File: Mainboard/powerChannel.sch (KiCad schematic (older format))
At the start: 2 parts, among them Q5 IRL640

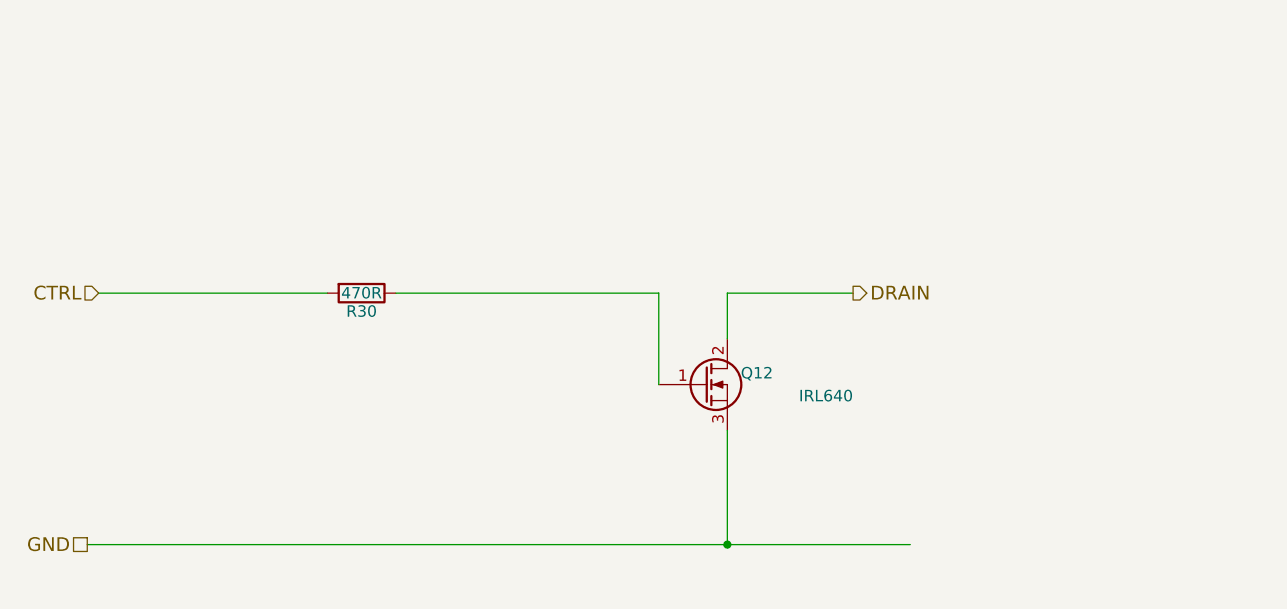
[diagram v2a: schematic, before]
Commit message: Made I2C level converters more neat
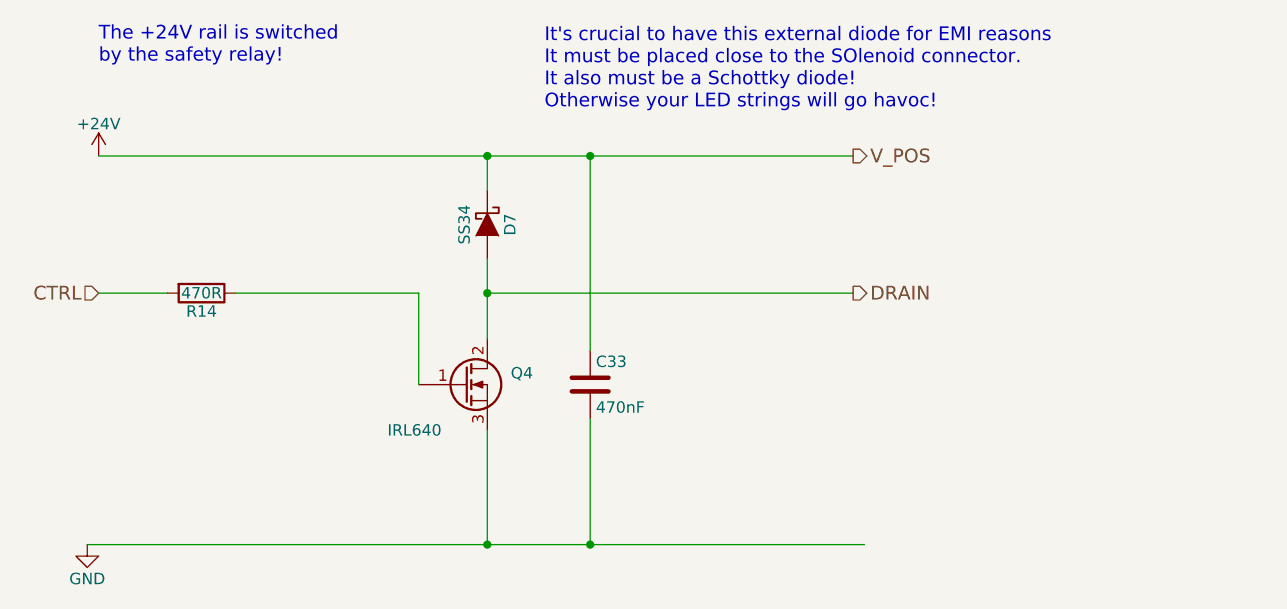
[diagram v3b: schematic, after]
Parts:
- added C25: 470nF, Capacitors_SMD:C_0805_HandSoldering, symbol C
- added D8: SS34, Diodes_SMD:SMC-RM10_Universal_Handsoldering, symbol D_Schottky
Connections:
- net labels added: +24V, V_POS
- wire segments 7 -> 11
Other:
- note added: "It's crucial to have this external diode for EMI reasons\nIt must be placed close to the SOlenoid connector.\nIt also must be a Schottky diode!\nOtherwise your LED strings will go havoc!"
- note added: "The +24V rail is switched\nby the safety relay!"
- moved on the sheet: Q4, R14
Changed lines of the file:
@@
 $Descr A4 11693 8268
 encoding utf-8
-Sheet 7 14
+Sheet 19 19
 Title ""
 Date ""
@@
 Text HLabel 1850 3600 0    60   Input ~ 0
 CTRL
-Text HLabel 1800 4700 0    60   UnSpc ~ 0
-GND
 Text HLabel 5150 3600 2    60   Output ~ 0
 DRAIN
 Wire Wire Line
-	1800 4700 5400 4700
-Wire Wire Line
-	4600 4200 4600 4700
-Connection ~ 4600 4700
-Wire Wire Line
-	4600 3800 4600 3600
-Wire Wire Line
-	4600 3600 5150 3600
-Wire Wire Line
-	4300 3600 4300 4000
+	1800 4700 5200 4700
+Wire Wire Line
+	3550 4200 3550 4700
+Connection ~ 3550 4700
+Wire Wire Line
+	3550 3450 3550 3800
+Wire Wire Line
+	3250 3600 3250 4000
 $Comp
 L R R23
 U 1 1 567075BF
-P 3000 3600
+P 2300 3600
 AR Path="/56721A83/567075BF" Ref="R23"  Part="1"
 AR Path="/56721A88/567075BF" Ref="R24"  Part="1"
@@
 AR Path="/56723FA7/567075BF" Ref="R29"  Part="1"
 AR Path="/56723FAC/567075BF" Ref="R30"  Part="1"
-F 0 "R30" V 3080 3600 50  0000 C CNN
-F 1 "470R" V 3000 3600 50  0000 C CNN
-F 2 "Resistors_SMD:R_0805_HandSoldering" V 2930 3600 50  0001 C CNN
-F 3 "" H 3000 3600 50  0000 C CNN
-	1    3000 3600
+AR Path="/57745597/567075BF" Ref="R24"  Part="1"
+AR Path="/577458A1/567075BF" Ref="R25"  Part="1"
+AR Path="/57745BCF/567075BF" Ref="R26"  Part="1"
+AR Path="/577510FE/567075BF" Ref="R27"  Part="1"
+AR Path="/57751111/567075BF" Ref="R28"  Part="1"
+AR Path="/57751116/567075BF" Ref="R29"  Part="1"
+AR Path="/5775111B/567075BF" Ref="R30"  Part="1"
+AR Path="/5770A9F1/567075BF" Ref="R1"  Part="1"
+AR Path="/5770AA04/567075BF" Ref="R24"  Part="1"
+AR Path="/5770AA09/567075BF" Ref="R24"  Part="1"
+AR Path="/5770AA0E/567075BF" Ref="R24"  Part="1"
+AR Path="/57714FDB/567075BF" Ref="R2"  Part="1"
+AR Path="/57715882/567075BF" Ref="R5"  Part="1"
+AR Path="/57715887/567075BF" Ref="R14"  Part="1"
+F 0 "R14" V 2380 3600 50  0000 C CNN
+F 1 "470R" V 2300 3600 50  0000 C CNN
+F 2 "Resistors_SMD:R_0805_HandSoldering" V 2230 3600 50  0001 C CNN
+F 3 "" H 2300 3600 50  0000 C CNN
+	1    2300 3600
 	0    1    1    0
 $EndComp
-Wire Wire Line
-	1850 3600 2850 3600
-Wire Wire Line
-	3150 3600 4300 3600
 $Comp
 L Q_NMOS_GDS Q5
 U 1 1 56763CC0
-P 4500 4000
+P 3450 4000
 AR Path="/56721A83/56763CC0" Ref="Q5"  Part="1"
 AR Path="/56721A88/56763CC0" Ref="Q6"  Part="1"
@@
 AR Path="/56723FA7/56763CC0" Ref="Q11"  Part="1"
 AR Path="/56723FAC/56763CC0" Ref="Q12"  Part="1"
-F 0 "Q12" H 4800 4050 50  0000 R CNN
-F 1 "IRL640" H 5150 3950 50  0000 R CNN
-F 2 "TO_SOT_Packages_THT:TO-220_Neutral123_Vertical_LargePads" H 4700 4100 50  0001 C CNN
-F 3 "" H 4500 4000 50  0000 C CNN
-	1    4500 4000
-	1    0    0    -1
-$EndComp
+AR Path="/57745597/56763CC0" Ref="Q6"  Part="1"
+AR Path="/577458A1/56763CC0" Ref="Q7"  Part="1"
+AR Path="/57745BCF/56763CC0" Ref="Q8"  Part="1"
+AR Path="/577510FE/56763CC0" Ref="Q9"  Part="1"
+AR Path="/57751111/56763CC0" Ref="Q10"  Part="1"
+AR Path="/57751116/56763CC0" Ref="Q11"  Part="1"
+AR Path="/5775111B/56763CC0" Ref="Q12"  Part="1"
+AR Path="/5770A9F1/56763CC0" Ref="Q1"  Part="1"
+AR Path="/5770AA04/56763CC0" Ref="Q6"  Part="1"
+AR Path="/5770AA09/56763CC0" Ref="Q6"  Part="1"
+AR Path="/5770AA0E/56763CC0" Ref="Q6"  Part="1"
+AR Path="/57714FDB/56763CC0" Ref="Q2"  Part="1"
+AR Path="/57715882/56763CC0" Ref="Q3"  Part="1"
+AR Path="/57715887/56763CC0" Ref="Q4"  Part="1"
+F 0 "Q4" H 3750 4050 50  0000 R CNN
+F 1 "IRL640" H 3350 3800 50  0000 R CNN
+F 2 "TO_SOT_Packages_THT:TO-220_Neutral123_Vertical_LargePads" H 3650 4100 50  0001 C CNN
+F 3 "" H 3450 4000 50  0000 C CNN
+	1    3450 4000
+	1    0    0    -1
+$EndComp
+Wire Wire Line
+	1850 3600 2150 3600
+Wire Wire Line
+	2450 3600 3250 3600
+Text Notes 3800 2800 0    60   ~ 0
+It's crucial to have this external diode for EMI reasons\nIt must be placed close to the SOlenoid connector.\nIt also must be a Schottky diode!\nOtherwise your LED strings will go havoc!
+Wire Wire Line
+	1850 3000 5150 3000
+Wire Wire Line
+	3550 3150 3550 3000
+Connection ~ 3550 3000
+$Comp
+L D_Schottky D8
+U 1 1 5772D520
+P 3550 3300
+AR Path="/56721A83/5772D520" Ref="D8"  Part="1"
+AR Path="/56721A88/5772D520" Ref="D?"  Part="1"
+AR Path="/57745597/5772D520" Ref="D9"  Part="1"
+AR Path="/577458A1/5772D520" Ref="D10"  Part="1"
+AR Path="/57745BCF/5772D520" Ref="D11"  Part="1"
+AR Path="/577510FE/5772D520" Ref="D13"  Part="1"
+AR Path="/57751111/5772D520" Ref="D14"  Part="1"
+AR Path="/57751116/5772D520" Ref="D15"  Part="1"
+AR Path="/5775111B/5772D520" Ref="D16"  Part="1"
+AR Path="/5770A9F1/5772D520" Ref="D4"  Part="1"
+AR Path="/5770AA04/5772D520" Ref="D9"  Part="1"
+AR Path="/5770AA09/5772D520" Ref="D9"  Part="1"
+AR Path="/5770AA0E/5772D520" Ref="D9"  Part="1"
+AR Path="/57714FDB/5772D520" Ref="D5"  Part="1"
+AR Path="/57715882/5772D520" Ref="D6"  Part="1"
+AR Path="/57715887/5772D520" Ref="D7"  Part="1"
+F 0 "D7" H 3550 3400 50  0000 C CNN
+F 1 "SS34" H 3550 3200 50  0000 C CNN
+F 2 "Diodes_SMD:SMC-RM10_Universal_Handsoldering" H 3550 3300 50  0001 C CNN
+F 3 "" H 3550 3300 50  0000 C CNN
+	1    3550 3300
+	0    1    1    0
+$EndComp
+Wire Wire Line
+	3550 3600 5150 3600
+Connection ~ 3550 3600
+$Comp
+L +24V #PWR038
+U 1 1 5773C3DD
+P 1850 3000
+AR Path="/56721A83/5773C3DD" Ref="#PWR038"  Part="1"
+AR Path="/56721A88/5773C3DD" Ref="#PWR?"  Part="1"
+AR Path="/57745597/5773C3DD" Ref="#PWR064"  Part="1"
+AR Path="/577458A1/5773C3DD" Ref="#PWR066"  Part="1"
+AR Path="/57745BCF/5773C3DD" Ref="#PWR068"  Part="1"
+AR Path="/577510FE/5773C3DD" Ref="#PWR070"  Part="1"
+AR Path="/57751111/5773C3DD" Ref="#PWR072"  Part="1"
+AR Path="/57751116/5773C3DD" Ref="#PWR074"  Part="1"
+AR Path="/5775111B/5773C3DD" Ref="#PWR076"  Part="1"
+AR Path="/5770A9F1/5773C3DD" Ref="#PWR078"  Part="1"
+AR Path="/5770AA04/5773C3DD" Ref="#PWR78"  Part="1"
+AR Path="/5770AA09/5773C3DD" Ref="#PWR80"  Part="1"
+AR Path="/5770AA0E/5773C3DD" Ref="#PWR82"  Part="1"
+AR Path="/57714FDB/5773C3DD" Ref="#PWR080"  Part="1"
+AR Path="/57715882/5773C3DD" Ref="#PWR082"  Part="1"
+AR Path="/57715887/5773C3DD" Ref="#PWR084"  Part="1"
+F 0 "#PWR084" H 1850 2850 50  0001 C CNN
+F 1 "+24V" H 1850 3140 50  0000 C CNN
+F 2 "" H 1850 3000 50  0000 C CNN
+F 3 "" H 1850 3000 50  0000 C CNN
+	1    1850 3000
+	1    0    0    -1
+$EndComp
+Text HLabel 5150 3000 2    60   Output ~ 0
+V_POS
+Text Notes 1850 2600 0    60   ~ 0
+The +24V rail is switched\nby the safety relay!
+$Comp
+L GND #PWR039
+U 1 1 5773D70E
+P 1800 4700
+AR Path="/56721A83/5773D70E" Ref="#PWR039"  Part="1"
+AR Path="/57745597/5773D70E" Ref="#PWR065"  Part="1"
+AR Path="/577458A1/5773D70E" Ref="#PWR067"  Part="1"
+AR Path="/57745BCF/5773D70E" Ref="#PWR069"  Part="1"
+AR Path="/577510FE/5773D70E" Ref="#PWR071"  Part="1"
+AR Path="/57751111/5773D70E" Ref="#PWR073"  Part="1"
+AR Path="/57751116/5773D70E" Ref="#PWR075"  Part="1"
+AR Path="/5775111B/5773D70E" Ref="#PWR077"  Part="1"
+AR Path="/5770A9F1/5773D70E" Ref="#PWR079"  Part="1"
+AR Path="/5770AA04/5773D70E" Ref="#PWR77"  Part="1"
+AR Path="/5770AA09/5773D70E" Ref="#PWR79"  Part="1"
+AR Path="/5770AA0E/5773D70E" Ref="#PWR81"  Part="1"
+AR Path="/57714FDB/5773D70E" Ref="#PWR081"  Part="1"
+AR Path="/57715882/5773D70E" Ref="#PWR083"  Part="1"
+AR Path="/57715887/5773D70E" Ref="#PWR085"  Part="1"
+F 0 "#PWR085" H 1800 4450 50  0001 C CNN
+F 1 "GND" H 1800 4550 50  0000 C CNN
+F 2 "" H 1800 4700 50  0000 C CNN
+F 3 "" H 1800 4700 50  0000 C CNN
+	1    1800 4700
+	1    0    0    -1
+$EndComp
+$Comp
+L C C25
+U 1 1 5774C3F2
+P 4000 4000
+AR Path="/56721A83/5774C3F2" Ref="C25"  Part="1"
+AR Path="/57745597/5774C3F2" Ref="C26"  Part="1"
+AR Path="/577458A1/5774C3F2" Ref="C27"  Part="1"
+AR Path="/57745BCF/5774C3F2" Ref="C28"  Part="1"
+AR Path="/577510FE/5774C3F2" Ref="C29"  Part="1"
+AR Path="/57751111/5774C3F2" Ref="C30"  Part="1"
+AR Path="/57751116/5774C3F2" Ref="C31"  Part="1"
+AR Path="/5775111B/5774C3F2" Ref="C32"  Part="1"
+AR Path="/5770A9F1/5774C3F2" Ref="C12"  Part="1"
+AR Path="/5770AA04/5774C3F2" Ref="C26"  Part="1"
+AR Path="/5770AA09/5774C3F2" Ref="C26"  Part="1"
+AR Path="/5770AA0E/5774C3F2" Ref="C26"  Part="1"
+AR Path="/57714FDB/5774C3F2" Ref="C14"  Part="1"
+AR Path="/57715882/5774C3F2" Ref="C15"  Part="1"
+AR Path="/57715887/5774C3F2" Ref="C33"  Part="1"
+F 0 "C33" H 4025 4100 50  0000 L CNN
+F 1 "470nF" H 4025 3900 50  0000 L CNN
+F 2 "Capacitors_SMD:C_0805_HandSoldering" H 4038 3850 50  0001 C CNN
+F 3 "" H 4000 4000 50  0000 C CNN
+	1    4000 4000
+	1    0    0    -1
+$EndComp
+Connection ~ 4000 3000
+Wire Wire Line
+	4000 3850 4000 3000
+Wire Wire Line
+	4000 4150 4000 4700
+Connection ~ 4000 4700
 $EndSCHEMATC

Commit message: Added 8 additional Mosfet channels, cleaned up rouing a bit
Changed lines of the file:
@@
 $Descr A4 11693 8268
 encoding utf-8
-Sheet 19 19
+Sheet 27 27
 Title ""
 Date ""
@@
 AR Path="/57715882/567075BF" Ref="R5"  Part="1"
 AR Path="/57715887/567075BF" Ref="R14"  Part="1"
-F 0 "R14" V 2380 3600 50  0000 C CNN
+AR Path="/578BB179/567075BF" Ref="R49"  Part="1"
+AR Path="/578BB1C5/567075BF" Ref="R50"  Part="1"
+AR Path="/578BB1CA/567075BF" Ref="R51"  Part="1"
+AR Path="/578BB1CF/567075BF" Ref="R52"  Part="1"
+AR Path="/578BB1E4/567075BF" Ref="R53"  Part="1"
+AR Path="/578BB1F3/567075BF" Ref="R54"  Part="1"
+AR Path="/578BB1F8/567075BF" Ref="R55"  Part="1"
+AR Path="/578BB1FD/567075BF" Ref="R56"  Part="1"
+F 0 "R56" V 2380 3600 50  0000 C CNN
 F 1 "470R" V 2300 3600 50  0000 C CNN
 F 2 "Resistors_SMD:R_0805_HandSoldering" V 2230 3600 50  0001 C CNN
@@
 AR Path="/57715882/56763CC0" Ref="Q3"  Part="1"
 AR Path="/57715887/56763CC0" Ref="Q4"  Part="1"
-F 0 "Q4" H 3750 4050 50  0000 R CNN
+AR Path="/578BB179/56763CC0" Ref="Q13"  Part="1"
+AR Path="/578BB1C5/56763CC0" Ref="Q14"  Part="1"
+AR Path="/578BB1CA/56763CC0" Ref="Q15"  Part="1"
+AR Path="/578BB1CF/56763CC0" Ref="Q16"  Part="1"
+AR Path="/578BB1E4/56763CC0" Ref="Q17"  Part="1"
+AR Path="/578BB1F3/56763CC0" Ref="Q18"  Part="1"
+AR Path="/578BB1F8/56763CC0" Ref="Q19"  Part="1"
+AR Path="/578BB1FD/56763CC0" Ref="Q20"  Part="1"
+F 0 "Q20" H 3750 4050 50  0000 R CNN
 F 1 "IRL640" H 3350 3800 50  0000 R CNN
 F 2 "TO_SOT_Packages_THT:TO-220_Neutral123_Vertical_LargePads" H 3650 4100 50  0001 C CNN
@@
 AR Path="/577458A1/5772D520" Ref="D10"  Part="1"
 AR Path="/57745BCF/5772D520" Ref="D11"  Part="1"
-AR Path="/577510FE/5772D520" Ref="D13"  Part="1"
-AR Path="/57751111/5772D520" Ref="D14"  Part="1"
-AR Path="/57751116/5772D520" Ref="D15"  Part="1"
-AR Path="/5775111B/5772D520" Ref="D16"  Part="1"
+AR Path="/577510FE/5772D520" Ref="D12"  Part="1"
+AR Path="/57751111/5772D520" Ref="D13"  Part="1"
+AR Path="/57751116/5772D520" Ref="D14"  Part="1"
+AR Path="/5775111B/5772D520" Ref="D15"  Part="1"
 AR Path="/5770A9F1/5772D520" Ref="D4"  Part="1"
 AR Path="/5770AA04/5772D520" Ref="D9"  Part="1"
@@
 AR Path="/57715882/5772D520" Ref="D6"  Part="1"
 AR Path="/57715887/5772D520" Ref="D7"  Part="1"
-F 0 "D7" H 3550 3400 50  0000 C CNN
+AR Path="/578BB179/5772D520" Ref="D16"  Part="1"
+AR Path="/578BB1C5/5772D520" Ref="D17"  Part="1"
+AR Path="/578BB1CA/5772D520" Ref="D18"  Part="1"
+AR Path="/578BB1CF/5772D520" Ref="D19"  Part="1"
+AR Path="/578BB1E4/5772D520" Ref="D20"  Part="1"
+AR Path="/578BB1F3/5772D520" Ref="D21"  Part="1"
+AR Path="/578BB1F8/5772D520" Ref="D22"  Part="1"
+AR Path="/578BB1FD/5772D520" Ref="D23"  Part="1"
+F 0 "D23" V 3550 3400 50  0000 C CNN
 F 1 "SS34" H 3550 3200 50  0000 C CNN
 F 2 "Diodes_SMD:SMC-RM10_Universal_Handsoldering" H 3550 3300 50  0001 C CNN
@@
 Connection ~ 3550 3600
 $Comp
-L +24V #PWR038
+L +24V #PWR043
 U 1 1 5773C3DD
 P 1850 3000
-AR Path="/56721A83/5773C3DD" Ref="#PWR038"  Part="1"
+AR Path="/56721A83/5773C3DD" Ref="#PWR043"  Part="1"
 AR Path="/56721A88/5773C3DD" Ref="#PWR?"  Part="1"
-AR Path="/57745597/5773C3DD" Ref="#PWR064"  Part="1"
-AR Path="/577458A1/5773C3DD" Ref="#PWR066"  Part="1"
-AR Path="/57745BCF/5773C3DD" Ref="#PWR068"  Part="1"
-AR Path="/577510FE/5773C3DD" Ref="#PWR070"  Part="1"
-AR Path="/57751111/5773C3DD" Ref="#PWR072"  Part="1"
-AR Path="/57751116/5773C3DD" Ref="#PWR074"  Part="1"
-AR Path="/5775111B/5773C3DD" Ref="#PWR076"  Part="1"
-AR Path="/5770A9F1/5773C3DD" Ref="#PWR078"  Part="1"
+AR Path="/57745597/5773C3DD" Ref="#PWR070"  Part="1"
+AR Path="/577458A1/5773C3DD" Ref="#PWR072"  Part="1"
+AR Path="/57745BCF/5773C3DD" Ref="#PWR074"  Part="1"
+AR Path="/577510FE/5773C3DD" Ref="#PWR076"  Part="1"
+AR Path="/57751111/5773C3DD" Ref="#PWR078"  Part="1"
+AR Path="/57751116/5773C3DD" Ref="#PWR080"  Part="1"
+AR Path="/5775111B/5773C3DD" Ref="#PWR082"  Part="1"
+AR Path="/5770A9F1/5773C3DD" Ref="#PWR084"  Part="1"
 AR Path="/5770AA04/5773C3DD" Ref="#PWR78"  Part="1"
 AR Path="/5770AA09/5773C3DD" Ref="#PWR80"  Part="1"
 AR Path="/5770AA0E/5773C3DD" Ref="#PWR82"  Part="1"
-AR Path="/57714FDB/5773C3DD" Ref="#PWR080"  Part="1"
-AR Path="/57715882/5773C3DD" Ref="#PWR082"  Part="1"
-AR Path="/57715887/5773C3DD" Ref="#PWR084"  Part="1"
-F 0 "#PWR084" H 1850 2850 50  0001 C CNN
+AR Path="/57714FDB/5773C3DD" Ref="#PWR086"  Part="1"
+AR Path="/57715882/5773C3DD" Ref="#PWR088"  Part="1"
+AR Path="/57715887/5773C3DD" Ref="#PWR090"  Part="1"
+AR Path="/578BB179/5773C3DD" Ref="#PWR092"  Part="1"
+AR Path="/578BB1C5/5773C3DD" Ref="#PWR094"  Part="1"
+AR Path="/578BB1CA/5773C3DD" Ref="#PWR096"  Part="1"
+AR Path="/578BB1CF/5773C3DD" Ref="#PWR098"  Part="1"
+AR Path="/578BB1E4/5773C3DD" Ref="#PWR0100"  Part="1"
+AR Path="/578BB1F3/5773C3DD" Ref="#PWR0102"  Part="1"
+AR Path="/578BB1F8/5773C3DD" Ref="#PWR0104"  Part="1"
+AR Path="/578BB1FD/5773C3DD" Ref="#PWR0106"  Part="1"
+F 0 "#PWR0106" H 1850 2850 50  0001 C CNN
 F 1 "+24V" H 1850 3140 50  0000 C CNN
 F 2 "" H 1850 3000 50  0000 C CNN
@@
 The +24V rail is switched\nby the safety relay!
 $Comp
-L GND #PWR039
+L GND #PWR044
 U 1 1 5773D70E
 P 1800 4700
-AR Path="/56721A83/5773D70E" Ref="#PWR039"  Part="1"
-AR Path="/57745597/5773D70E" Ref="#PWR065"  Part="1"
-AR Path="/577458A1/5773D70E" Ref="#PWR067"  Part="1"
-AR Path="/57745BCF/5773D70E" Ref="#PWR069"  Part="1"
-AR Path="/577510FE/5773D70E" Ref="#PWR071"  Part="1"
-AR Path="/57751111/5773D70E" Ref="#PWR073"  Part="1"
-AR Path="/57751116/5773D70E" Ref="#PWR075"  Part="1"
-AR Path="/5775111B/5773D70E" Ref="#PWR077"  Part="1"
-AR Path="/5770A9F1/5773D70E" Ref="#PWR079"  Part="1"
+AR Path="/56721A83/5773D70E" Ref="#PWR044"  Part="1"
+AR Path="/57745597/5773D70E" Ref="#PWR071"  Part="1"
+AR Path="/577458A1/5773D70E" Ref="#PWR073"  Part="1"
+AR Path="/57745BCF/5773D70E" Ref="#PWR075"  Part="1"
+AR Path="/577510FE/5773D70E" Ref="#PWR077"  Part="1"
+AR Path="/57751111/5773D70E" Ref="#PWR079"  Part="1"
+AR Path="/57751116/5773D70E" Ref="#PWR081"  Part="1"
+AR Path="/5775111B/5773D70E" Ref="#PWR083"  Part="1"
+AR Path="/5770A9F1/5773D70E" Ref="#PWR085"  Part="1"
 AR Path="/5770AA04/5773D70E" Ref="#PWR77"  Part="1"
 AR Path="/5770AA09/5773D70E" Ref="#PWR79"  Part="1"
 AR Path="/5770AA0E/5773D70E" Ref="#PWR81"  Part="1"
-AR Path="/57714FDB/5773D70E" Ref="#PWR081"  Part="1"
-AR Path="/57715882/5773D70E" Ref="#PWR083"  Part="1"
-AR Path="/57715887/5773D70E" Ref="#PWR085"  Part="1"
-F 0 "#PWR085" H 1800 4450 50  0001 C CNN
+AR Path="/57714FDB/5773D70E" Ref="#PWR087"  Part="1"
+AR Path="/57715882/5773D70E" Ref="#PWR089"  Part="1"
+AR Path="/57715887/5773D70E" Ref="#PWR091"  Part="1"
+AR Path="/578BB179/5773D70E" Ref="#PWR093"  Part="1"
+AR Path="/578BB1C5/5773D70E" Ref="#PWR095"  Part="1"
+AR Path="/578BB1CA/5773D70E" Ref="#PWR097"  Part="1"
+AR Path="/578BB1CF/5773D70E" Ref="#PWR099"  Part="1"
+AR Path="/578BB1E4/5773D70E" Ref="#PWR0101"  Part="1"
+AR Path="/578BB1F3/5773D70E" Ref="#PWR0103"  Part="1"
+AR Path="/578BB1F8/5773D70E" Ref="#PWR0105"  Part="1"
+AR Path="/578BB1FD/5773D70E" Ref="#PWR0107"  Part="1"
+F 0 "#PWR0107" H 1800 4450 50  0001 C CNN
 F 1 "GND" H 1800 4550 50  0000 C CNN
 F 2 "" H 1800 4700 50  0000 C CNN
@@
 AR Path="/57714FDB/5774C3F2" Ref="C14"  Part="1"
 AR Path="/57715882/5774C3F2" Ref="C15"  Part="1"
-AR Path="/57715887/5774C3F2" Ref="C33"  Part="1"
-F 0 "C33" H 4025 4100 50  0000 L CNN
+AR Path="/57715887/5774C3F2" Ref="C42"  Part="1"
+AR Path="/578BB179/5774C3F2" Ref="C33"  Part="1"
+AR Path="/578BB1C5/5774C3F2" Ref="C34"  Part="1"
+AR Path="/578BB1CA/5774C3F2" Ref="C35"  Part="1"
+AR Path="/578BB1CF/5774C3F2" Ref="C36"  Part="1"
+AR Path="/578BB1E4/5774C3F2" Ref="C37"  Part="1"
+AR Path="/578BB1F3/5774C3F2" Ref="C38"  Part="1"
+AR Path="/578BB1F8/5774C3F2" Ref="C39"  Part="1"
+AR Path="/578BB1FD/5774C3F2" Ref="C40"  Part="1"
+F 0 "C40" H 4050 4150 50  0000 L CNN
 F 1 "470nF" H 4025 3900 50  0000 L CNN
 F 2 "Capacitors_SMD:C_0805_HandSoldering" H 4038 3850 50  0001 C CNN
